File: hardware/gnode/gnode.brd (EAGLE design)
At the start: 50 x 25 mm, 25 parts, among them IC1 HTU21D, U1 ATMEGA328P_TQFP

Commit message: tidying. ready to go
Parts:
- moved C2 0.25 mm to (11.4, 17.8)
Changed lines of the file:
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@@
 <element name="JP1" library="SparkFun-Connectors" package="2X3_LOCK" value="AVR_SPI_PRG_62X3_LOCK" x="22.352" y="2.286"/>
 <element name="U$3" library="dtb" package="SOT23" value="MCP1700TT" x="8.89" y="21.844" rot="R90"/>
-<element name="C2" library="passives-7351" package="C0603-N" value="1u" x="11.43" y="18.034" rot="R180"/>
+<element name="C2" library="passives-7351" package="C0603-N" value="1u" x="11.43" y="17.78" rot="R180"/>
 <element name="U$4" library="jonsowman" package="SOIC8" value="CN3083" x="16.51" y="11.938" rot="R180"/>
 <element name="JP2" library="Mine" package="1X02" value="" x="9.398" y="10.16" rot="R315"/>
@@
 <wire x1="6.35" y1="10.668" x2="10.16" y2="6.858" width="0.508" layer="1"/>
 <wire x1="7.79" y1="21.844" x2="7.79" y2="18.024996875" width="0.508" layer="1"/>
-<wire x1="12.23" y1="18.034" x2="12.23" y2="19.634" width="0.254" layer="1"/>
+<wire x1="12.23" y1="17.78" x2="12.23" y2="19.634" width="0.254" layer="1"/>
 <wire x1="12.23" y1="19.634" x2="12.535" y2="19.939" width="0.254" layer="1"/>
 <wire x1="7.79" y1="21.844" x2="10.922" y2="21.844" width="0.254" layer="1"/>

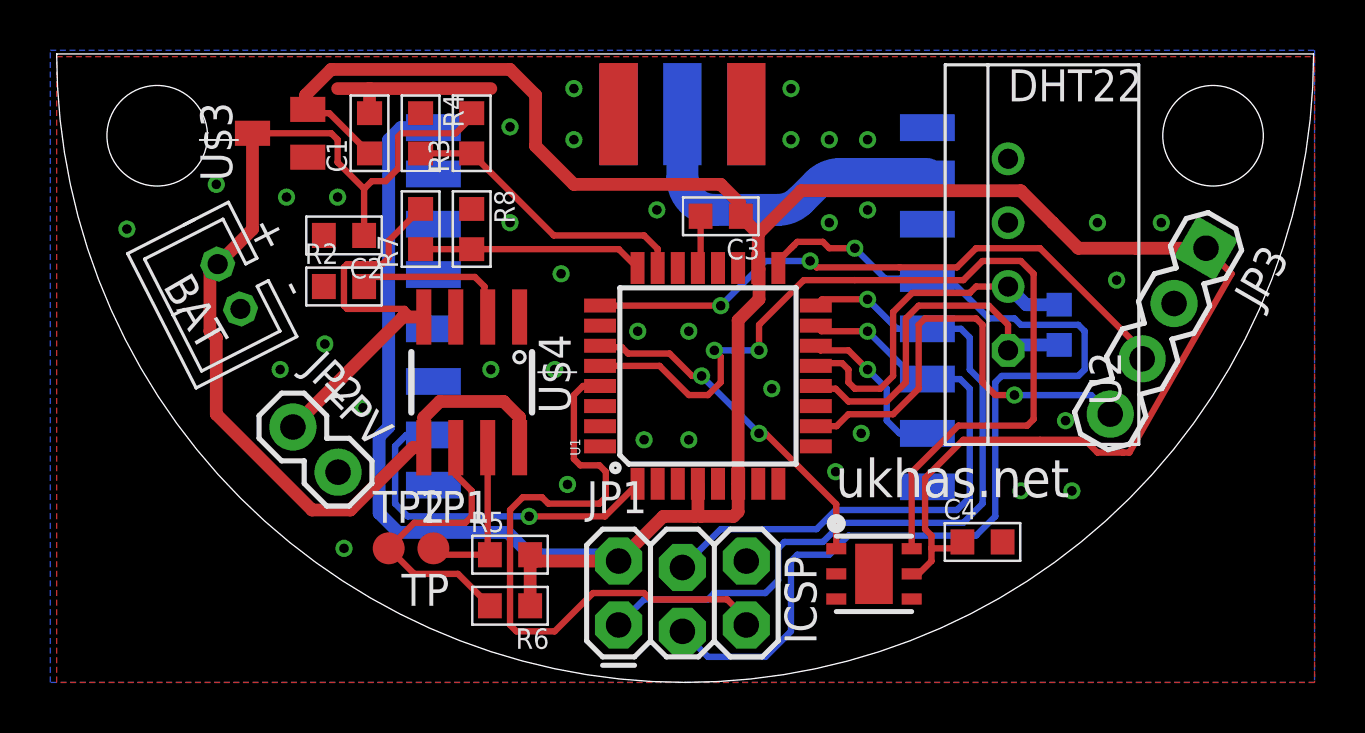
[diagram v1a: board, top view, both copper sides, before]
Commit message: added RC for rain sensing. part numbers on silk
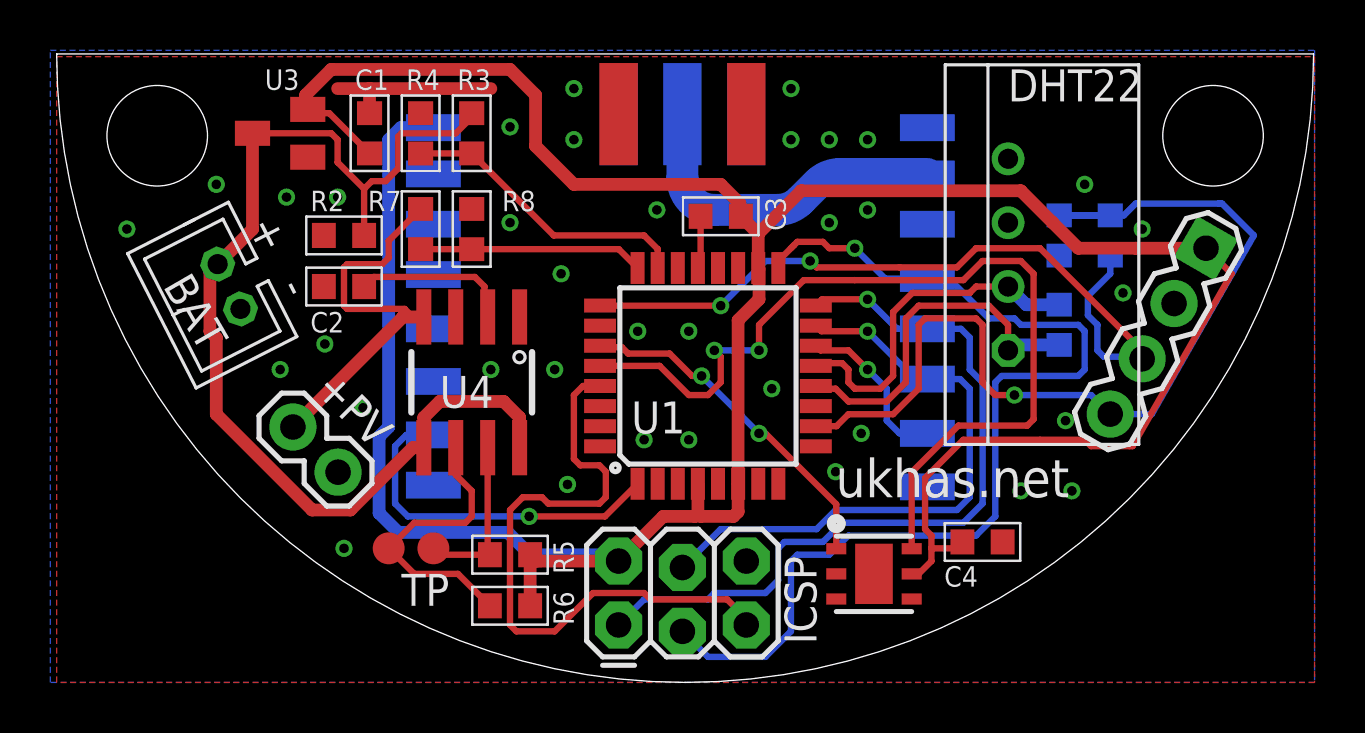
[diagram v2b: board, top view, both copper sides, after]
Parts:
- added C5: 100n, passives-7351:C0603-N
- added R9: (no value), passives-7351:R0603-N
- renumbered IC1 to U5, U$3 to U3, U$4 to U4
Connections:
- net GND: now also C5.2
- net GPIO0: now also C5.1, R9.1
- net GPIO1: now also R9.2
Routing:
- net GPIO0: track 17.9 -> 38.2 mm
- net GPIO1: track 24.7 -> 31.0 mm

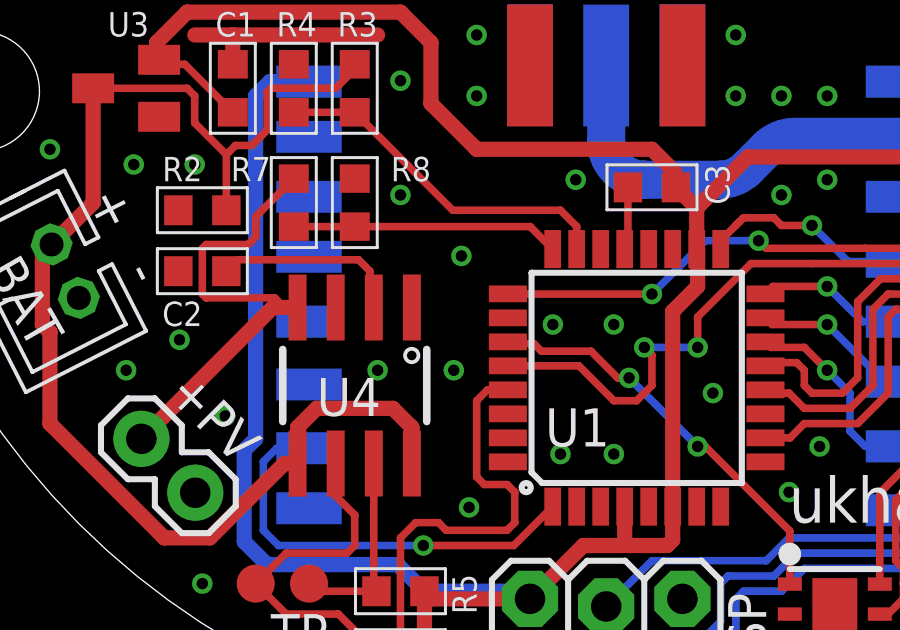
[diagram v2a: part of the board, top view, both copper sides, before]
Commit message: ISET connected to ADC pin so we can calculate the charge current
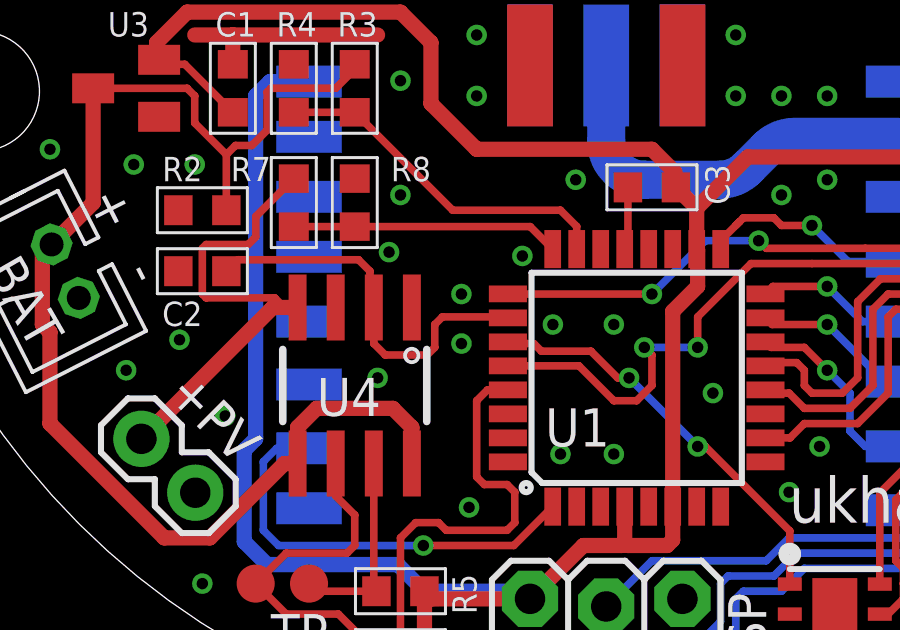
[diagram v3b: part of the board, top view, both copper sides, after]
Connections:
- removed net N$4: R2.2, U4.2
- new net ISET: R2.2, U1.26, U4.2
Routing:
- net ISET: track 0.00 -> 13.2 mm
- net N$4: track 6.37 -> 0.00 mm
- net GND: vias 36 -> 38
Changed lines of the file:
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@@
 <layer number="23" name="tOrigins" color="15" fill="1" visible="yes" active="yes"/>
 <layer number="24" name="bOrigins" color="15" fill="1" visible="yes" active="yes"/>
-<layer number="25" name="tNames" color="7" fill="1" visible="yes" active="yes"/>
-<layer number="26" name="bNames" color="7" fill="1" visible="yes" active="yes"/>
+<layer number="25" name="tNames" color="7" fill="1" visible="no" active="yes"/>
+<layer number="26" name="bNames" color="7" fill="1" visible="no" active="yes"/>
 <layer number="27" name="tValues" color="7" fill="1" visible="no" active="yes"/>
 <layer number="28" name="bValues" color="7" fill="1" visible="no" active="yes"/>
@@
 <layer number="47" name="Measures" color="7" fill="1" visible="no" active="yes"/>
 <layer number="48" name="Document" color="7" fill="1" visible="no" active="yes"/>
-<layer number="49" name="Reference" color="7" fill="1" visible="yes" active="yes"/>
+<layer number="49" name="Reference" color="7" fill="1" visible="no" active="yes"/>
 <layer number="50" name="dxf" color="7" fill="1" visible="no" active="no"/>
 <layer number="51" name="tDocu" color="6" fill="1" visible="yes" active="yes"/>
@@
 <via x="9.144" y="19.304" extent="1-16" drill="0.381"/>
 <via x="11.176" y="19.304" extent="1-16" drill="0.381"/>
-<via x="17.272" y="12.446" extent="1-16" drill="0.381"/>
+<via x="17.272" y="12.192" extent="1-16" drill="0.381"/>
 <via x="12.192" y="10.922" extent="1-16" drill="0.381"/>
 <via x="11.43" y="5.334" extent="1-16" drill="0.381"/>
-<via x="20.066" y="16.256" extent="1-16" drill="0.381"/>
-<via x="19.812" y="12.446" extent="1-16" drill="0.381"/>
+<via x="22.098" y="16.256" extent="1-16" drill="0.381"/>
+<via x="20.066" y="13.335" extent="1-16" drill="0.381"/>
 <via x="20.32" y="7.874" extent="1-16" drill="0.381"/>
 <wire x1="11.176" y1="23.622" x2="12.446" y2="23.622" width="0.508" layer="1"/>
@@
 <via x="43.18" y="18.034" extent="1-16" drill="0.381"/>
 <contactref element="C5" pad="2"/>
+<via x="20.066" y="14.986" extent="1-16" drill="0.381"/>
+<via x="17.653" y="16.383" extent="1-16" drill="0.381"/>
 </signal>
 <signal name="N$1">
@@
 <wire x1="21.6154" y1="11.792" x2="20.936" y2="11.792" width="0.254" layer="1"/>
 </signal>
-<signal name="N$4">
-<contactref element="U4" pad="2"/>
-<contactref element="R2" pad="2"/>
-<wire x1="12.23" y1="15.748" x2="12.611" y2="16.129" width="0.254" layer="1"/>
-<wire x1="12.611" y1="16.129" x2="16.637" y2="16.129" width="0.254" layer="1"/>
-<wire x1="17.145" y1="14.538" x2="17.018" y2="14.665" width="0.254" layer="1"/>
-<wire x1="17.018" y1="14.665" x2="17.018" y2="15.748" width="0.254" layer="1"/>
-<wire x1="17.018" y1="15.748" x2="16.637" y2="16.129" width="0.254" layer="1"/>
-</signal>
 <signal name="N$2">
 <contactref element="U4" pad="7"/>
@@
 <wire x1="46.355" y1="19.05" x2="47.625" y2="17.78" width="0.254" layer="16"/>
 </signal>
+<signal name="ISET">
+<contactref element="U1" pad="26"/>
+<contactref element="U4" pad="2"/>
+<contactref element="R2" pad="2"/>
+<wire x1="12.23" y1="15.748" x2="12.611" y2="16.129" width="0.254" layer="1"/>
+<wire x1="12.611" y1="16.129" x2="16.637" y2="16.129" width="0.254" layer="1"/>
+<wire x1="17.145" y1="14.538" x2="17.018" y2="14.665" width="0.254" layer="1"/>
+<wire x1="17.018" y1="14.665" x2="17.018" y2="15.748" width="0.254" layer="1"/>
+<wire x1="17.018" y1="15.748" x2="16.637" y2="16.129" width="0.254" layer="1"/>
+<wire x1="17.145" y1="14.538" x2="17.145" y2="13.335" width="0.254" layer="1"/>
+<wire x1="17.145" y1="13.335" x2="17.526" y2="12.954" width="0.254" layer="1"/>
+<wire x1="17.526" y1="12.954" x2="18.923" y2="12.954" width="0.254" layer="1"/>
+<wire x1="18.923" y1="12.954" x2="19.177" y2="13.208" width="0.254" layer="1"/>
+<wire x1="19.177" y1="13.208" x2="19.177" y2="13.97" width="0.254" layer="1"/>
+<wire x1="19.177" y1="13.97" x2="19.431" y2="14.224" width="0.254" layer="1"/>
+<wire x1="19.431" y1="14.224" x2="21.5834" y2="14.224" width="0.254" layer="1"/>
+<wire x1="21.5834" y1="14.224" x2="21.6154" y2="14.192" width="0.254" layer="1"/>
+</signal>
 </signals>
